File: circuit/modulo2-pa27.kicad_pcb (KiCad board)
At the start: 2 copper layers, 105 x 47 mm, 48 parts, among them J1 CONN_01X02, J3 CONN_01X04, J4 JACK_MONO, J5 HOLE, J7 HOLE, SW1 bright, U1 OPA2134, U2 OPA2134, U3 TLE2426, U4 POWER

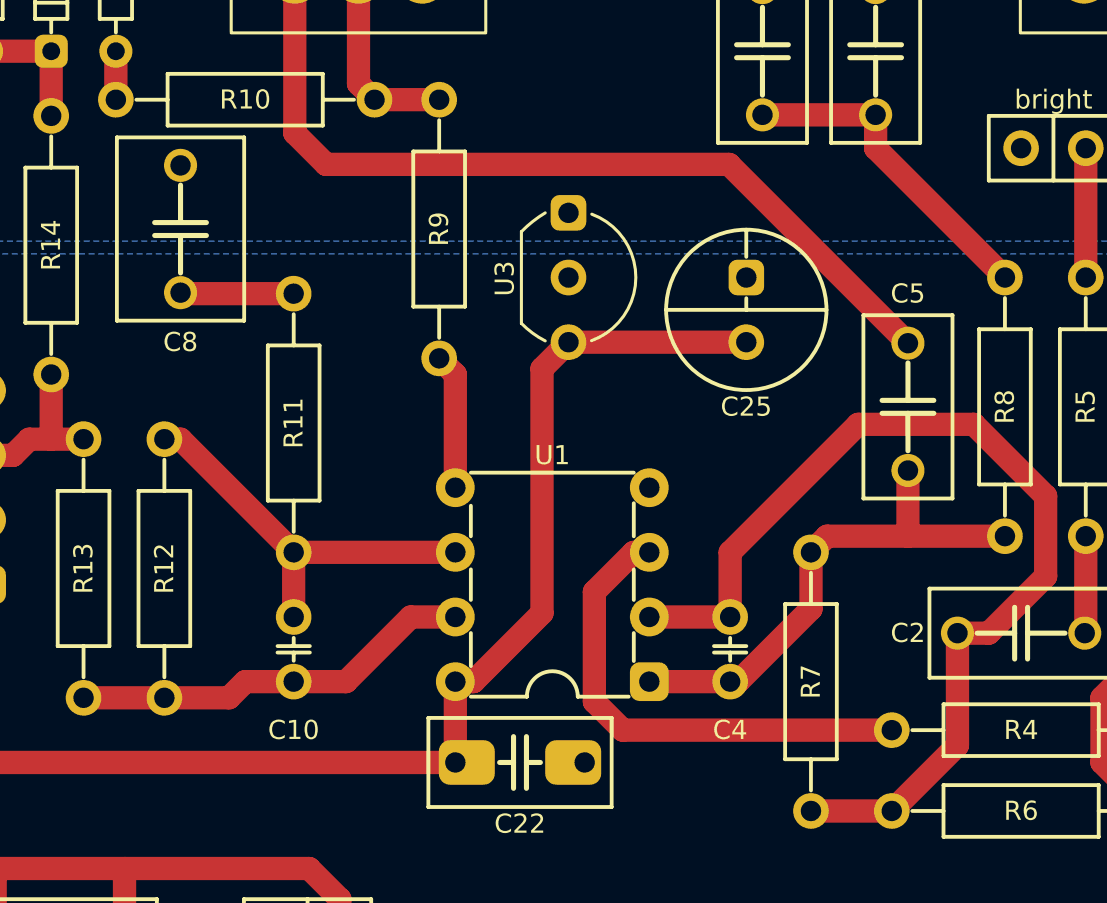
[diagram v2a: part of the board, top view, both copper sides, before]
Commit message: ditched the LED array board; LEDs are on the main PCB now
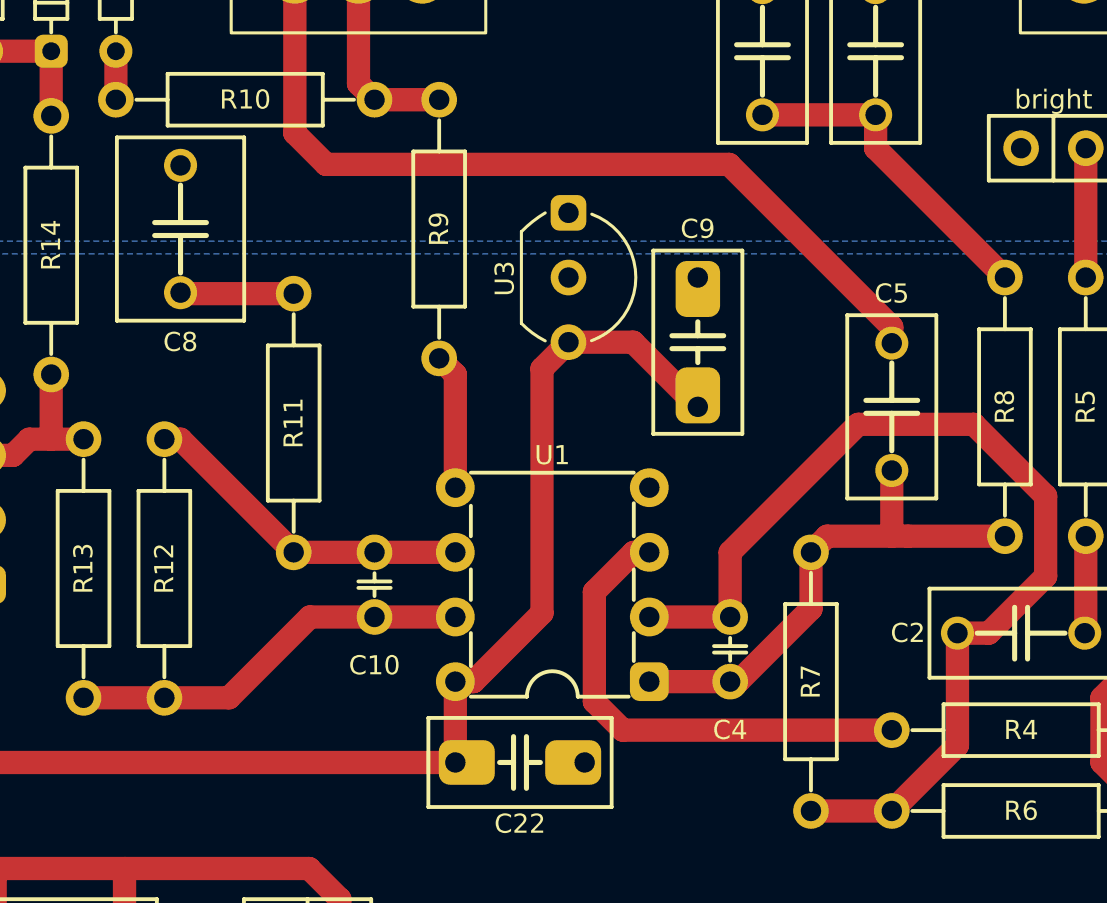
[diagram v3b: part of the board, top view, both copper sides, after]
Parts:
- removed C25: 47u, myAmp:CPOL_D6.3_P2.5
- added C9: 100nF, myAmp:C_5MM_1206, F.Cu at (100.3, 69.8)
- C10, C4: value 120p -> 120pF
- C2: value 22n -> 22nF
- C24: value 47u -> 47µF
- C3, C8: value 1u -> 1µF
- C5: value 250p -> 250pF
- C6: value 100n -> 100nF
- C7: value 47n -> 47nF
- U4: value POWER -> PWR_CONN
- moved C10 4.07 mm to (87.6, 79.4)
- moved C5 0.63 mm to (108.0, 72.4)
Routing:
- net Net-(C10-Pad1): track 15.8 -> 13.3 mm
- net +24V: track 70.8 -> 70.0 mm
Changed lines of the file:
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@@
       (effects (font (size 0.75 0.75) (thickness 0.15)))
     )
-    (fp_text value "1u" (at -1.016 -0.254 90) (layer "F.Fab") hide
+    (fp_text value "1µF" (at -1.016 -0.254 90) (layer "F.Fab") hide
       (effects (font (size 0.0254 0.0254) (thickness 0.001)))
     )
@@
       (effects (font (size 0.75 0.75) (thickness 0.15)))
     )
-    (fp_text value "120p" (at -0.5715 -0.381 90) (layer "F.Fab") hide
+    (fp_text value "120pF" (at -0.5715 -0.381 90) (layer "F.Fab") hide
       (effects (font (size 0.03 0.03) (thickness 0.001)))
     )
@@
   )
   (footprint "myAmp:C_FILM_L7.2mm_W3.5mm_P5.00mm" (layer "F.Cu")
-    (at 108.585 72.39 90)
+    (at 107.95 72.39 90)
     (property "Sheetfile" "modulo2-pa27.kicad_sch")
     (property "Sheetname" "")
@@
       (effects (font (size 0.75 0.75) (thickness 0.15)))
     )
-    (fp_text value "250p" (at -1.016 -0.254 90) (layer "F.Fab") hide
+    (fp_text value "250pF" (at -1.016 -0.254 90) (layer "F.Fab") hide
       (effects (font (size 0.0254 0.0254) (thickness 0.001)))
     )
@@
       (effects (font (size 0.75 0.75) (thickness 0.15)))
     )
-    (fp_text value "22n" (at -1.016 -0.254) (layer "F.Fab") hide
+    (fp_text value "22nF" (at -1.016 -0.254) (layer "F.Fab") hide
       (effects (font (size 0.0254 0.0254) (thickness 0.001)))
     )
@@
       (effects (font (size 0.75 0.75) (thickness 0.15)))
     )
-    (fp_text value "100n" (at -1.016 -0.254 90) (layer "F.Fab") hide
+    (fp_text value "100nF" (at -1.016 -0.254 90) (layer "F.Fab") hide
       (effects (font (size 0.0254 0.0254) (thickness 0.001)))
     )
@@
       (effects (font (size 0.75 0.75) (thickness 0.15)))
     )
-    (fp_text value "47n" (at -1.016 -0.254 90) (layer "F.Fab") hide
+    (fp_text value "47nF" (at -1.016 -0.254 90) (layer "F.Fab") hide
       (effects (font (size 0.0254 0.0254) (thickness 0.001)))
     )
@@
       (effects (font (size 0.75 0.75) (thickness 0.15)))
     )
-    (fp_text value "1u" (at -1.016 -0.254 90) (layer "F.Fab") hide
+    (fp_text value "1µF" (at -1.016 -0.254 90) (layer "F.Fab") hide
       (effects (font (size 0.0254 0.0254) (thickness 0.001)))
     )
@@
       (effects (font (size 0.75 0.75) (thickness 0.15)))
     )
-    (fp_text value "POWER" (at 2.54 -0.635) (layer "F.Fab") hide
+    (fp_text value "PWR_CONN" (at 2.54 -0.635) (layer "F.Fab") hide
       (effects (font (size 0.03 0.03) (thickness 0.0075)))
     )
@@
     )
   )
-  (footprint "myAmp:CPOL_D6.3_P2.5" (layer "F.Cu")
-    (at 102.235 68.58 90)
-    (property "Sheetfile" "modulo2-pa27.kicad_sch")
-    (property "Sheetname" "")
-    (attr through_hole)
-    (fp_text reference "C25" (at -3.81 0) (layer "F.SilkS")
-      (effects (font (size 0.75 0.75) (thickness 0.15)))
-    )
-    (fp_text value "47u" (at 1 -2 90) (layer "F.Fab")
-      (effects (font (size 0.127 0.127) (thickness 0.03175)))
-    )
-    (fp_line (start 0 -3.15) (end 0 3.15) (layer "F.SilkS") (width 0.15))
-    (fp_line (start 0 0) (end 0.4572 0) (layer "F.SilkS") (width 0.15))
-    (fp_line (start 3.15 0) (end 2.0828 0) (layer "F.SilkS") (width 0.15))
-    (fp_circle (center 0 0) (end 3.15 0) (layer "F.SilkS") (width 0.15) (fill none))
-    (pad "1" thru_hole circle (at -1.27 0 90) (size 1.4 1.4) (drill 0.8) (layers *.Cu *.Mask)
+  (footprint "myAmp:C_5MM_1206" (layer "F.Cu")
+    (at 100.33 69.85 -90)
+    (property "Sheetfile" "modulo2-pa27.kicad_sch")
+    (property "Sheetname" "")
+    (attr through_hole)
+    (fp_text reference "C9" (at -4.445 0 180) (layer "F.SilkS")
+      (effects (font (size 0.75 0.75) (thickness 0.15)))
+    )
+    (fp_text value "100nF" (at -1.016 -0.254 90) (layer "F.Fab") hide
+      (effects (font (size 0.127 0.127) (thickness 0.001)))
+    )
+    (fp_line (start -3.6 -1.75) (end 3.6 -1.75) (layer "F.SilkS") (width 0.15))
+    (fp_line (start -3.6 -1.75) (end -3.6 1.75) (layer "F.SilkS") (width 0.15))
+    (fp_line (start -0.254 0) (end -0.8 0) (layer "F.SilkS") (width 0.2))
+    (fp_line (start 0.254 0) (end 0.8 0) (layer "F.SilkS") (width 0.2))
+    (fp_line (start -0.254 -1.016) (end -0.254 1.016) (layer "F.SilkS") (width 0.2))
+    (fp_line (start 0.254 -1.016) (end 0.254 1.016) (layer "F.SilkS") (width 0.2))
+    (fp_line (start 3.6 1.75) (end 3.6 -1.75) (layer "F.SilkS") (width 0.15))
+    (fp_line (start -3.6 1.75) (end 3.6 1.75) (layer "F.SilkS") (width 0.15))
+    (pad "1" thru_hole roundrect locked (at -2.54 0 270) (size 2.2 1.75) (drill 0.8 (offset 0.45 0)) (layers *.Cu *.Mask) (roundrect_rratio 0.25)
+      (net 2 "GND") (pintype "passive"))
+    (pad "2" thru_hole roundrect locked (at 2.54 0 270) (size 2.2 1.75) (drill 0.8 (offset -0.45 0)) (layers *.Cu *.Mask) (roundrect_rratio 0.25)
       (net 1 "+24V") (pintype "passive"))
-    (pad "2" thru_hole roundrect (at 1.27 0 90) (size 1.4 1.4) (drill 0.8) (layers *.Cu *.Mask) (roundrect_rratio 0.25)
-      (net 2 "GND") (pintype "passive"))
-    (model "${KIPRJMOD}/myAmp.pretty/models/CP_Radial_D6.3mm_P2.50mm.step"
-      (offset (xyz -1.25 0 0))
+    (model "${KIPRJMOD}/myAmp.pretty/models/C_Disc_D5.1mm_W3.2mm_P5.00mm.step"
+      (offset (xyz -2.5 0 0))
       (scale (xyz 1 1 1))
       (rotate (xyz 0 0 0))
@@
   )
   (footprint "myAmp:C_2.5MM" (layer "F.Cu")
-    (at 84.455 81.915 -90)
+    (at 87.63 79.375 -90)
     (property "Sheetfile" "modulo2-pa27.kicad_sch")
     (property "Sheetname" "")
@@
       (effects (font (size 0.75 0.75) (thickness 0.15)))
     )
-    (fp_text value "120p" (at -0.5715 -0.381 90) (layer "F.Fab") hide
+    (fp_text value "120pF" (at -0.5715 -0.381 90) (layer "F.Fab") hide
       (effects (font (size 0.03 0.03) (thickness 0.001)))
     )
@@
       (effects (font (size 0.75 0.75) (thickness 0.15)))
     )
-    (fp_text value "47u" (at 1 -2) (layer "F.Fab")
+    (fp_text value "47µF" (at 1 -2) (layer "F.Fab")
       (effects (font (size 0.127 0.127) (thickness 0.03175)))
     )
@@
   )
   (segment (start 94.2086 70.8914) (end 94.2086 80.4926) (width 0.9144) (layer "F.Cu") (net 1))
+  (segment (start 100.33 72.39) (end 97.79 69.85) (width 0.9144) (layer "F.Cu") (net 1))
   (segment (start 90.805 83.185) (end 90.805 86.36) (width 0.9144) (layer "F.Cu") (net 1))
   (segment (start 94.2086 80.4926) (end 91.5162 83.185) (width 0.9144) (layer "F.Cu") (net 1))
   (segment (start 60.96 82.55) (end 61.976 82.55) (width 0.9144) (layer "F.Cu") (net 1))
-  (segment (start 102.235 69.85) (end 95.25 69.85) (width 0.9144) (layer "F.Cu") (net 1))
   (segment (start 64.77 82.55) (end 68.58 86.36) (width 0.9144) (layer "F.Cu") (net 1))
   (segment (start 95.25 69.85) (end 94.2086 70.8914) (width 0.9144) (layer "F.Cu") (net 1))
+  (segment (start 97.79 69.85) (end 95.25 69.85) (width 0.9144) (layer "F.Cu") (net 1))
   (segment (start 61.976 82.55) (end 64.77 82.55) (width 0.9144) (layer "F.Cu") (net 1))
   (segment (start 91.5162 83.185) (end 90.805 83.185) (width 0.9144) (layer "F.Cu") (net 1))
@@
   (segment (start 108.585 77.47) (end 105.41 77.47) (width 0.9144) (layer "F.Cu") (net 10))
   (segment (start 112.395 77.47) (end 108.585 77.47) (width 0.9144) (layer "F.Cu") (net 10))
-  (segment (start 108.585 74.89) (end 108.585 77.47) (width 0.9144) (layer "F.Cu") (net 10))
+  (segment (start 107.95 74.89) (end 107.95 77.47) (width 0.9144) (layer "F.Cu") (net 10))
   (segment (start 104.775 80.3275) (end 104.775 78.105) (width 0.9144) (layer "F.Cu") (net 10))
   (segment (start 98.425 83.185) (end 101.6 83.185) (width 0.9144) (layer "F.Cu") (net 10))
@@
   (segment (start 80.01 73.66) (end 84.455 78.105) (width 0.9144) (layer "F.Cu") (net 12))
   (segment (start 79.375 73.66) (end 80.01 73.66) (width 0.9144) (layer "F.Cu") (net 12))
-  (segment (start 84.455 80.645) (end 84.455 78.105) (width 0.9144) (layer "F.Cu") (net 12))
-  (segment (start 84.455 83.185) (end 82.55 83.185) (width 0.9144) (layer "F.Cu") (net 13))
-  (segment (start 84.455 83.185) (end 86.5124 83.185) (width 0.9144) (layer "F.Cu") (net 13))
-  (segment (start 81.915 83.82) (end 79.375 83.82) (width 0.9144) (layer "F.Cu") (net 13))
-  (segment (start 86.5124 83.185) (end 89.0524 80.645) (width 0.9144) (layer "F.Cu") (net 13))
+  (segment (start 85.09 80.645) (end 87.63 80.645) (width 0.9144) (layer "F.Cu") (net 13))
+  (segment (start 87.63 80.645) (end 90.805 80.645) (width 0.9144) (layer "F.Cu") (net 13))
   (segment (start 76.2 83.82) (end 79.375 83.82) (width 0.9144) (layer "F.Cu") (net 13))
-  (segment (start 89.0524 80.645) (end 90.805 80.645) (width 0.9144) (layer "F.Cu") (net 13))
-  (segment (start 82.55 83.185) (end 81.915 83.82) (width 0.9144) (layer "F.Cu") (net 13))
+  (segment (start 79.375 83.82) (end 81.915 83.82) (width 0.9144) (layer "F.Cu") (net 13))
+  (segment (start 81.915 83.82) (end 85.09 80.645) (width 0.9144) (layer "F.Cu") (net 13))
   (segment (start 70.2056 90.5256) (end 67.945 88.265) (width 0.9144) (layer "F.Cu") (net 14))
   (segment (start 77.81 90.5412) (end 77.8256 90.5256) (width 0.9144) (layer "F.Cu") (net 14))
@@
   (segment (start 115.57 67.31) (end 115.57 62.23) (width 0.9144) (layer "F.Cu") (net 30))
   (segment (start 101.56 62.865) (end 85.725 62.865) (width 0.9144) (layer "F.Cu") (net 31))
+  (segment (start 107.95 69.255) (end 101.56 62.865) (width 0.9144) (layer "F.Cu") (net 31))
+  (segment (start 107.95 69.89) (end 107.95 69.255) (width 0.9144) (layer "F.Cu") (net 31))
   (segment (start 85.725 62.865) (end 84.5 61.64) (width 0.9144) (layer "F.Cu") (net 31))
-  (segment (start 108.585 69.89) (end 101.56 62.865) (width 0.9144) (layer "F.Cu") (net 31))
   (segment (start 84.5 61.64) (end 84.5 55.55) (width 0.9144) (layer "F.Cu") (net 31))
   (segment (start 89.5 55.55) (end 89.87 55.92) (width 0.9144) (layer "F.Cu") (net 32))

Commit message: almost there...
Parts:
- C3, C8: footprint myAmp:C_FILM_L7.2mm_W5.5mm_P5.00mm -> myAmp:C_FILM_L7.2mm_W5.0mm_P5.00mm
- moved C8 0.64 mm to (80.0, 66.0)
- moved C3 0.63 mm to (121.3, 66.0)
- moved RV2 0.26 mm to (149.0, 55.4)
- moved RV1 0.15 mm to (87.0, 55.4)
- moved RV3 0.15 mm to (118.0, 55.4)
- moved RV5 0.15 mm to (56.0, 55.4)
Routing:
- net Net-(RV5-Pad3): track 39.8 -> 39.1 mm
- net Net-(C3-Pad2): track 22.0 -> 22.6 mm

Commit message: sent to fab!
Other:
- board text added: "2022/2/27"
- board text added: "bass"
- board text added: "mid"
- board text added: "treb"
- board text added: "vol"
- board text removed: "2022/03/06"
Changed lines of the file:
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@@
     (pad_to_mask_clearance 0)
     (pcbplotparams
-      (layerselection 0x0000000_7fffffff)
+      (layerselection 0x00010f0_ffffffff)
       (disableapertmacros false)
-      (usegerberextensions false)
+      (usegerberextensions true)
       (usegerberattributes true)
       (usegerberadvancedattributes true)
@@
       (sketchpadsonfab false)
       (subtractmaskfromsilk false)
-      (outputformat 5)
+      (outputformat 1)
       (mirror false)
       (drillshape 0)
       (scaleselection 1)
-      (outputdirectory "")
+      (outputdirectory "gerber/")
     )
   )
@@
     (effects (font (size 0.75 0.75) (thickness 0.15)) (justify right))
   )
-  (gr_text "2022/03/06" (at 110.49 93.98) (layer "F.SilkS")
+  (gr_text "2022/2/27" (at 110.49 93.98) (layer "F.SilkS")
     (effects (font (size 2 2) (thickness 0.3)))
+  )
+  (gr_text "vol" (at 63.5 52.07) (layer "F.SilkS")
+    (effects (font (size 1.5 1.5) (thickness 0.3)))
   )
   (gr_text "GND" (at 83.7438 94.2848 90) (layer "F.SilkS")
     (effects (font (size 0.75 0.75) (thickness 0.15)) (justify right))
   )
+  (gr_text "mid" (at 125.73 52.07) (layer "F.SilkS")
+    (effects (font (size 1.5 1.5) (thickness 0.3)))
+  )
   (gr_text "OUT" (at 86.3092 94.3864 90) (layer "F.SilkS")
     (effects (font (size 0.75 0.75) (thickness 0.15)) (justify right))
@@
     (effects (font (size 0.75 0.75) (thickness 0.15)) (justify right))
   )
+  (gr_text "bass" (at 140.97 52.07) (layer "F.SilkS")
+    (effects (font (size 1.5 1.5) (thickness 0.3)))
+  )
   (gr_text "modulo2-pa27" (at 135.255 93.98) (layer "F.SilkS")
     (effects (font (size 2 2) (thickness 0.3)))
@@
     (effects (font (size 0.75 0.75) (thickness 0.15)) (justify right))
   )
+  (gr_text "treb" (at 95.25 52.07) (layer "F.SilkS")
+    (effects (font (size 1.5 1.5) (thickness 0.3)))
+  )
   (segment (start 94.2086 70.8914) (end 94.2086 80.4926) (width 0.9144) (layer "F.Cu") (net 1))
